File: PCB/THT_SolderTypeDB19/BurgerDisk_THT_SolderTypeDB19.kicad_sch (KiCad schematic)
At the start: 15 parts, among them J1 Daisy port in, J2 MicroSD module, J3 UART, J4 Daisy port out, U1 PC817

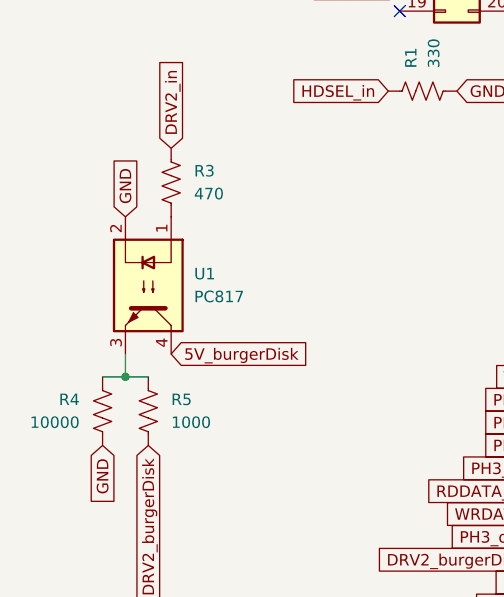
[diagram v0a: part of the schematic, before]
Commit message: Reverse 3 resistors for correct silkscreen orientation
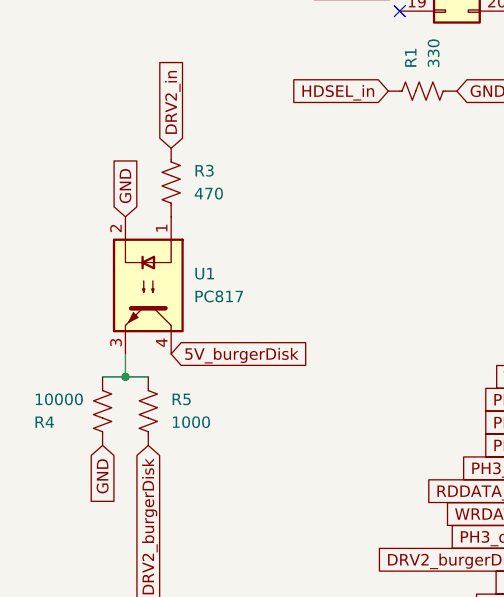
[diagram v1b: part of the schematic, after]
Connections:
- net DRV2_burgerDisk: now also R5.1; no longer R5.2
- net DRV2_in: now also R3.1; no longer R3.2
- net GND: now also R4.1; no longer R4.2
- net at U1.1: now also R3.2; no longer R3.1
- new net: R4.2, R5.2, U1.3
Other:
- moved on the sheet: R3, R4, R5
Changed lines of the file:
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@@
     )
   )
-  (symbol (lib_id "Device:R_US") (at 91.44 93.98 0) (unit 1)
+  (symbol (lib_id "Device:R_US") (at 91.44 93.98 180) (unit 1)
     (in_bom yes) (on_board yes) (dnp no)
-    (property "Reference" "R4" (at 88.9 92.71 0)
-      (effects (font (size 1.27 1.27)) (justify right))
-    )
-    (property "Value" "10000" (at 88.9 95.25 0)
-      (effects (font (size 1.27 1.27)) (justify right))
-    )
-    (property "Footprint" "Resistor_THT:R_Axial_DIN0207_L6.3mm_D2.5mm_P7.62mm_Horizontal" (at 92.456 94.234 90)
+    (property "Reference" "R4" (at 83.82 95.25 0)
+      (effects (font (size 1.27 1.27)) (justify right))
+    )
+    (property "Value" "10000" (at 83.82 92.71 0)
+      (effects (font (size 1.27 1.27)) (justify right))
+    )
+    (property "Footprint" "Resistor_THT:R_Axial_DIN0207_L6.3mm_D2.5mm_P7.62mm_Horizontal" (at 90.424 93.726 90)
       (effects (font (size 1.27 1.27)) hide)
     )
@@
     )
   )
-  (symbol (lib_id "Device:R_US") (at 99.06 68.58 180) (unit 1)
+  (symbol (lib_id "Device:R_US") (at 99.06 68.58 0) (unit 1)
     (in_bom yes) (on_board yes) (dnp no) (fields_autoplaced)
     (property "Reference" "R3" (at 101.6 67.31 0)
-      (effects (font (size 1.27 1.27)) (justify right))
+      (effects (font (size 1.27 1.27)) (justify left))
     )
     (property "Value" "470" (at 101.6 69.85 0)
-      (effects (font (size 1.27 1.27)) (justify right))
-    )
-    (property "Footprint" "Resistor_THT:R_Axial_DIN0309_L9.0mm_D3.2mm_P12.70mm_Horizontal" (at 98.044 68.326 90)
+      (effects (font (size 1.27 1.27)) (justify left))
+    )
+    (property "Footprint" "Resistor_THT:R_Axial_DIN0309_L9.0mm_D3.2mm_P12.70mm_Horizontal" (at 100.076 68.834 90)
       (effects (font (size 1.27 1.27)) hide)
     )
@@
     )
   )
-  (symbol (lib_id "Device:R_US") (at 96.52 93.98 0) (unit 1)
+  (symbol (lib_id "Device:R_US") (at 96.52 93.98 180) (unit 1)
     (in_bom yes) (on_board yes) (dnp no) (fields_autoplaced)
     (property "Reference" "R5" (at 99.06 92.71 0)
-      (effects (font (size 1.27 1.27)) (justify left))
+      (effects (font (size 1.27 1.27)) (justify right))
     )
     (property "Value" "1000" (at 99.06 95.25 0)
-      (effects (font (size 1.27 1.27)) (justify left))
-    )
-    (property "Footprint" "Resistor_THT:R_Axial_DIN0207_L6.3mm_D2.5mm_P7.62mm_Horizontal" (at 97.536 94.234 90)
-      (effects (font (size 1.27 1.27)) hide)
-    )
+      (effects (font (size 1.27 1.27)) (justify right))
+    )
+    (property "Footprint" "Resistor_THT:R_Axial_DIN0207_L6.3mm_D2.5mm_P7.62mm_Horizontal" (at 95.504 93.726 90)
+      (effects (font (size 1.27 1.27)) hide)
+    )

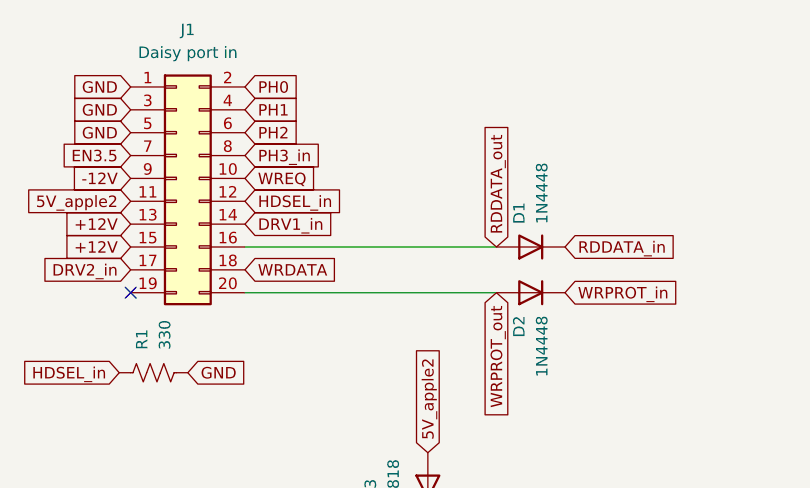
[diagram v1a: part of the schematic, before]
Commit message: Remove RDDATA diode, causing harm on SoftSP
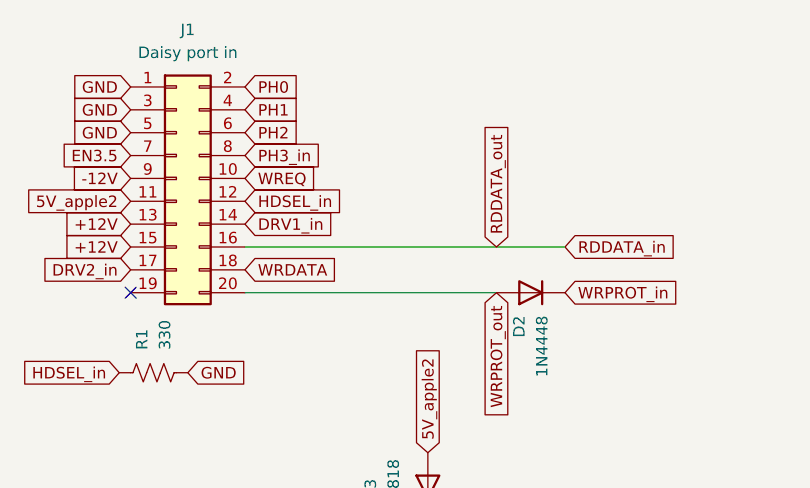
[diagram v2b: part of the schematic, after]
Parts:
- removed D1: 1N4448, Diode_THT:D_DO-35_SOD27_P7.62mm_Horizontal, symbol Diode:1N4448
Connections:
- net RDDATA_out is gone; now on net RDDATA_in: J1.16 (Pin_16), J4.18 (P18)

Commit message: Switch to cheaper IDC box header
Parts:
- J1: LCSC C17463886 -> C3405
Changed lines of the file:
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@@
 			)
 		)
-		(property "LCSC" "C17463886"
+		(property "LCSC" "C3405"
 			(at 129.54 36.83 0)
 			(effects
